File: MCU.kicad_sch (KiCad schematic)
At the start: 33 parts, among them J200 SWD, J201 USB_B_Micro, SW200 SW_SPDT, U200 STM32F405RGT6, U201 USBLC6-2SC6, Y200 16MHz

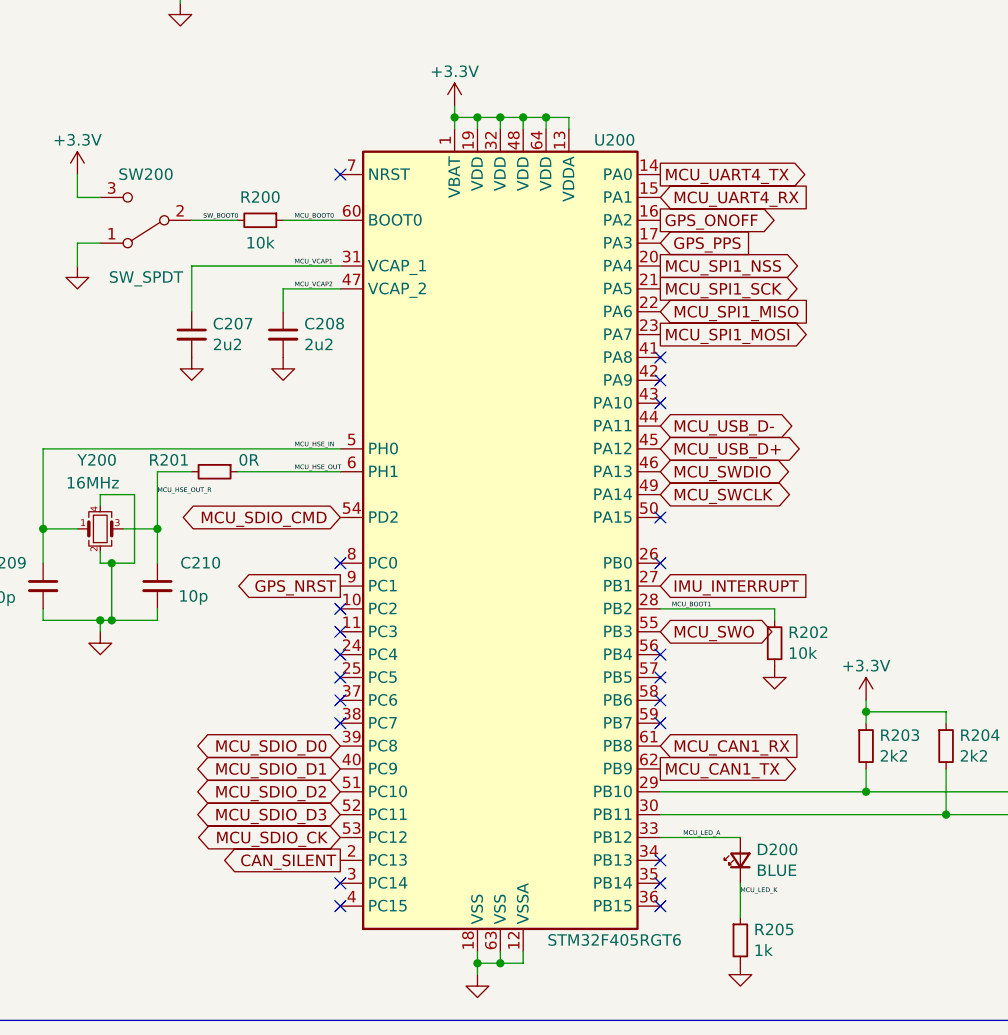
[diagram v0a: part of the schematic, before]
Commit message: replaced CAN transceiver, introduced new IMU
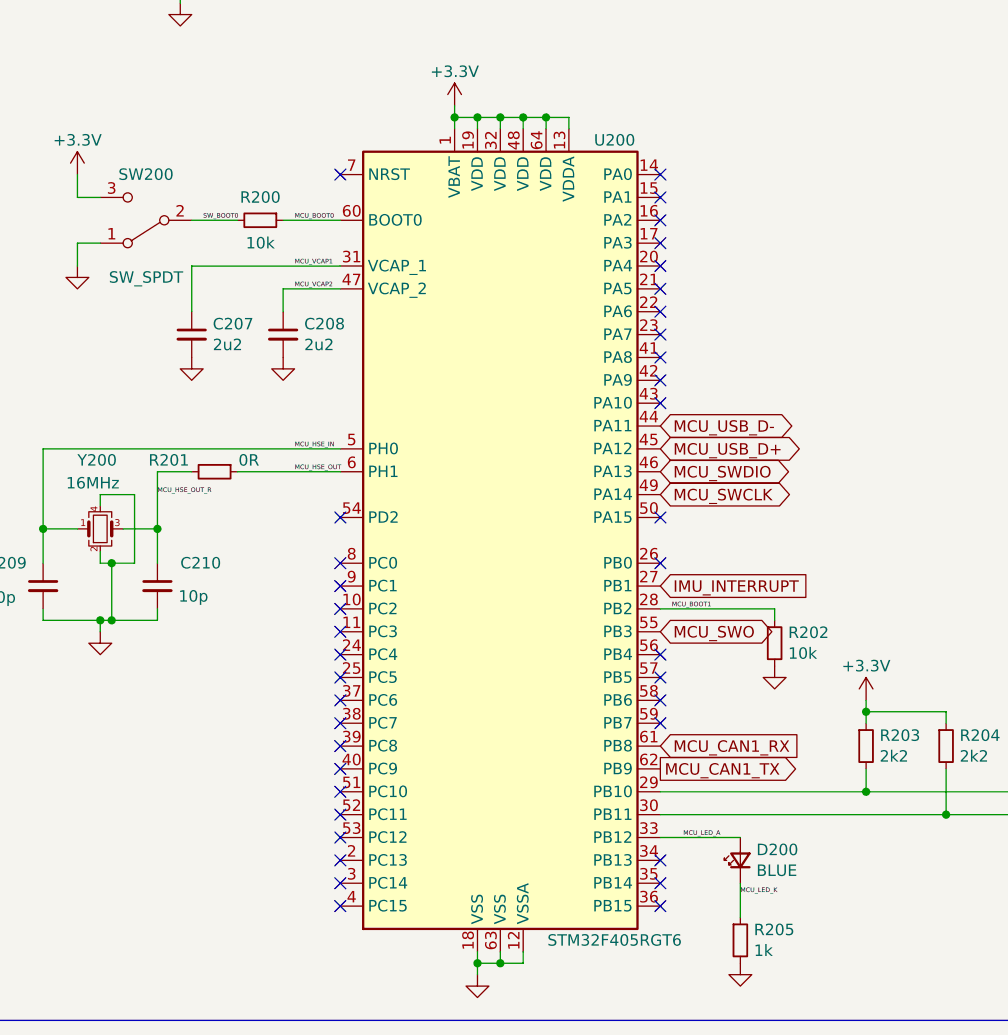
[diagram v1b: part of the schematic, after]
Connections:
- net CAN_SILENT: no longer names the net of U200.2 (PC13)
- net GPS_NRST: no longer names the net of U200.9 (PC1)
- net GPS_ONOFF: no longer names the net of U200.16 (PA2)
- net GPS_PPS: no longer names the net of U200.17 (PA3)
- net MCU_SDIO_CK: no longer names the net of U200.53 (PC12)
- net MCU_SDIO_CMD: no longer names the net of U200.54 (PD2)
- net MCU_SDIO_D0: no longer names the net of U200.39 (PC8)
- net MCU_SDIO_D1: no longer names the net of U200.40 (PC9)
- net MCU_SDIO_D2: no longer names the net of U200.51 (PC10)
- net MCU_SDIO_D3: no longer names the net of U200.52 (PC11)
- net MCU_SPI1_MISO: no longer names the net of U200.22 (PA6)
- net MCU_SPI1_MOSI: no longer names the net of U200.23 (PA7)
- net MCU_SPI1_NSS: no longer names the net of U200.20 (PA4)
- net MCU_SPI1_SCK: no longer names the net of U200.21 (PA5)
- net MCU_UART4_RX: no longer names the net of U200.15 (PA1)
- net MCU_UART4_TX: no longer names the net of U200.14 (PA0)
- no-connect marks 27 -> 43
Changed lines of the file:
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@@
   (no_connect (at 213.36 60.96))
   (no_connect (at 101.6 134.62))
+  (no_connect (at 66.04 116.84))
+  (no_connect (at 66.04 124.46))
+  (no_connect (at 66.04 142.24))
+  (no_connect (at 66.04 144.78))
+  (no_connect (at 66.04 147.32))
+  (no_connect (at 66.04 149.86))
+  (no_connect (at 66.04 152.4))
+  (no_connect (at 66.04 154.94))
+  (no_connect (at 101.6 86.36))
+  (no_connect (at 101.6 88.9))
+  (no_connect (at 101.6 91.44))
+  (no_connect (at 101.6 93.98))
+  (no_connect (at 101.6 96.52))
+  (no_connect (at 101.6 78.74))
+  (no_connect (at 101.6 81.28))
+  (no_connect (at 101.6 83.82))
   (no_connect (at 101.6 137.16))
   (no_connect (at 101.6 99.06))
@@
     )
   )
-  (global_label "MCU_SDIO_D1" (shape bidirectional) (at 66.04 144.78 180) (fields_autoplaced)
-    (effects (font (size 1.27 1.27)) (justify right))
-    (property "Intersheet References" "${INTERSHEET_REFS}" (id 0) (at 0 0 0)
-      (effects (font (size 1.27 1.27)) hide)
-    )
-  )
-  (global_label "MCU_UART4_TX" (shape output) (at 101.6 78.74 0) (fields_autoplaced)
-    (effects (font (size 1.27 1.27)) (justify left))
-    (property "Intersheet References" "${INTERSHEET_REFS}" (id 0) (at 0 0 0)
-      (effects (font (size 1.27 1.27)) hide)
-    )
-  )
   (global_label "MCU_SWO" (shape bidirectional) (at 254 55.88 0) (fields_autoplaced)
     (effects (font (size 1.27 1.27)) (justify left))
@@
     )
   )
-  (global_label "GPS_PPS" (shape input) (at 101.6 86.36 0) (fields_autoplaced)
-    (effects (font (size 1.27 1.27)) (justify left))
-    (property "Intersheet References" "${INTERSHEET_REFS}" (id 0) (at 0 0 0)
-      (effects (font (size 1.27 1.27)) hide)
-    )
-  )
   (global_label "MCU_CAN1_RX" (shape input) (at 101.6 142.24 0) (fields_autoplaced)
     (effects (font (size 1.27 1.27)) (justify left))
@@
     )
   )
-  (global_label "GPS_ONOFF" (shape output) (at 101.6 83.82 0) (fields_autoplaced)
-    (effects (font (size 1.27 1.27)) (justify left))
-    (property "Intersheet References" "${INTERSHEET_REFS}" (id 0) (at 0 0 0)
-      (effects (font (size 1.27 1.27)) hide)
-    )
-  )
   (global_label "MCU_SWO" (shape bidirectional) (at 101.6 129.54 0) (fields_autoplaced)
     (effects (font (size 1.27 1.27)) (justify left))
@@
   )
   (global_label "MCU_SWDIO" (shape bidirectional) (at 254 50.8 0) (fields_autoplaced)
-    (effects (font (size 1.27 1.27)) (justify left))
-    (property "Intersheet References" "${INTERSHEET_REFS}" (id 0) (at 0 0 0)
-      (effects (font (size 1.27 1.27)) hide)
-    )
-  )
-  (global_label "MCU_SDIO_D0" (shape bidirectional) (at 66.04 142.24 180) (fields_autoplaced)
-    (effects (font (size 1.27 1.27)) (justify right))
-    (property "Intersheet References" "${INTERSHEET_REFS}" (id 0) (at 0 0 0)
-      (effects (font (size 1.27 1.27)) hide)
-    )
-  )
-  (global_label "MCU_SDIO_D3" (shape bidirectional) (at 66.04 149.86 180) (fields_autoplaced)
-    (effects (font (size 1.27 1.27)) (justify right))
-    (property "Intersheet References" "${INTERSHEET_REFS}" (id 0) (at 0 0 0)
-      (effects (font (size 1.27 1.27)) hide)
-    )
-  )
-  (global_label "CAN_SILENT" (shape output) (at 66.04 154.94 180) (fields_autoplaced)
-    (effects (font (size 1.27 1.27)) (justify right))
-    (property "Intersheet References" "${INTERSHEET_REFS}" (id 0) (at 0 0 0)
-      (effects (font (size 1.27 1.27)) hide)
-    )
-  )
-  (global_label "MCU_UART4_RX" (shape input) (at 101.6 81.28 0) (fields_autoplaced)
     (effects (font (size 1.27 1.27)) (justify left))
     (property "Intersheet References" "${INTERSHEET_REFS}" (id 0) (at 0 0 0)
@@
     )
   )
-  (global_label "GPS_NRST" (shape output) (at 66.04 124.46 180) (fields_autoplaced)
-    (effects (font (size 1.27 1.27)) (justify right))
-    (property "Intersheet References" "${INTERSHEET_REFS}" (id 0) (at 0 0 0)
-      (effects (font (size 1.27 1.27)) hide)
-    )
-  )
   (global_label "CONN_USB_D+" (shape input) (at 252.73 118.11 180) (fields_autoplaced)
     (effects (font (size 1.27 1.27)) (justify right))
@@
     )
   )
-  (global_label "MCU_SPI1_MOSI" (shape output) (at 101.6 96.52 0) (fields_autoplaced)
-    (effects (font (size 1.27 1.27)) (justify left))
-    (property "Intersheet References" "${INTERSHEET_REFS}" (id 0) (at 0 0 0)
-      (effects (font (size 1.27 1.27)) hide)
-    )
-  )
-  (global_label "MCU_SPI1_SCK" (shape output) (at 101.6 91.44 0) (fields_autoplaced)
-    (effects (font (size 1.27 1.27)) (justify left))
-    (property "Intersheet References" "${INTERSHEET_REFS}" (id 0) (at 0 0 0)
-      (effects (font (size 1.27 1.27)) hide)
-    )
-  )
   (global_label "IMU_INTERRUPT" (shape input) (at 101.6 124.46 0) (fields_autoplaced)
     (effects (font (size 1.27 1.27)) (justify left))
@@
     )
   )
-  (global_label "MCU_SDIO_CMD" (shape bidirectional) (at 66.04 116.84 180) (fields_autoplaced)
-    (effects (font (size 1.27 1.27)) (justify right))
-    (property "Intersheet References" "${INTERSHEET_REFS}" (id 0) (at 0 0 0)
-      (effects (font (size 1.27 1.27)) hide)
-    )
-  )
   (global_label "MCU_I2C2_SDA" (shape bidirectional) (at 142.24 149.86 0) (fields_autoplaced)
     (effects (font (size 1.27 1.27)) (justify left))
@@
     )
   )
-  (global_label "MCU_SPI1_MISO" (shape input) (at 101.6 93.98 0) (fields_autoplaced)
-    (effects (font (size 1.27 1.27)) (justify left))
-    (property "Intersheet References" "${INTERSHEET_REFS}" (id 0) (at 0 0 0)
-      (effects (font (size 1.27 1.27)) hide)
-    )
-  )
   (global_label "MCU_USB_D+" (shape input) (at 210.82 116.84 0) (fields_autoplaced)
     (effects (font (size 1.27 1.27)) (justify left))
@@
     )
   )
-  (global_label "MCU_SDIO_D2" (shape bidirectional) (at 66.04 147.32 180) (fields_autoplaced)
-    (effects (font (size 1.27 1.27)) (justify right))
-    (property "Intersheet References" "${INTERSHEET_REFS}" (id 0) (at 0 0 0)
-      (effects (font (size 1.27 1.27)) hide)
-    )
-  )
-  (global_label "MCU_SDIO_CK" (shape bidirectional) (at 66.04 152.4 180) (fields_autoplaced)
-    (effects (font (size 1.27 1.27)) (justify right))
-    (property "Intersheet References" "${INTERSHEET_REFS}" (id 0) (at 0 0 0)
-      (effects (font (size 1.27 1.27)) hide)
-    )
-  )
   (global_label "MCU_SWCLK" (shape bidirectional) (at 254 53.34 0) (fields_autoplaced)
     (effects (font (size 1.27 1.27)) (justify left))
@@
     (effects (font (size 1.27 1.27)) (justify left))
     (property "Intersheet References" "${INTERSHEET_REFS}" (id 0) (at 0 0 0)
-      (effects (font (size 1.27 1.27)) hide)
-    )
-  )
-  (global_label "MCU_SPI1_NSS" (shape output) (at 101.6 88.9 0) (fields_autoplaced)
-    (effects (font (size 1.27 1.27)) (justify left))
-    (property "Intersheet References" "${INTERSHEET_REFS}" (id 0) (at 0 0 0)

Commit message: more changes!
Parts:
- added R1, R2: 2k2, Resistor_SMD:R_0402_1005Metric, symbol Device:R_Small
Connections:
- net +3V3: now also R1.1, R2.1
- net MCU_I2C1_SCL: now reaches U200.58 (PB6)
- net MCU_I2C1_SCL: now also R1.2
- net MCU_I2C1_SDA: now reaches U200.59 (PB7)
- net MCU_I2C1_SDA: now also R2.2
- no-connect marks 43 -> 41
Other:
- moved on the sheet: R202, R203, R204

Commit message: this is a message
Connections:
- net 14: now reaches U200.14 (PA0)
- net 15: now reaches U200.15 (PA1)
- net 16: now reaches U200.16 (PA2)
- net 17: now reaches U200.17 (PA3)
- net 20: now reaches U200.20 (PA4)
- net 21: now reaches U200.21 (PA5)
- net 22: now reaches U200.22 (PA6)
- net 23: now reaches U200.23 (PA7)
- net 24: now reaches U200.24 (PC4)
- net 25: now reaches U200.25 (PC5)
- net 26: now reaches U200.26 (PB0)
- net 41: now reaches U200.41 (PA8)
- net 42: now reaches U200.42 (PA9)
- net 43: now reaches U200.43 (PA10)
- net 50: now reaches U200.50 (PA15)
- no-connect marks 41 -> 26
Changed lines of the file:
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@@
   (no_connect (at 66.04 152.4))
   (no_connect (at 66.04 154.94))
-  (no_connect (at 101.6 86.36))
-  (no_connect (at 101.6 88.9))
-  (no_connect (at 101.6 91.44))
-  (no_connect (at 101.6 93.98))
-  (no_connect (at 101.6 96.52))
-  (no_connect (at 101.6 78.74))
-  (no_connect (at 101.6 81.28))
-  (no_connect (at 101.6 83.82))
-  (no_connect (at 101.6 99.06))
-  (no_connect (at 66.04 132.08))
   (no_connect (at 252.73 123.19))
   (no_connect (at 101.6 160.02))
-  (no_connect (at 101.6 101.6))
   (no_connect (at 200.66 58.42))
-  (no_connect (at 101.6 121.92))
   (no_connect (at 66.04 160.02))
   (no_connect (at 66.04 157.48))
@@
   (no_connect (at 66.04 137.16))
   (no_connect (at 213.36 58.42))
-  (no_connect (at 66.04 134.62))
-  (no_connect (at 101.6 116.84))
   (no_connect (at 66.04 129.54))
   (no_connect (at 101.6 157.48))
-  (no_connect (at 101.6 104.14))
   (no_connect (at 66.04 139.7))
   (no_connect (at 101.6 132.08))
@@
     (effects (font (size 0.508 0.508)) (justify left bottom))
   )
+  (global_label "50" (shape input) (at 101.6 116.84 0) (fields_autoplaced)
+    (effects (font (size 1.27 1.27)) (justify left))
+    (property "Intersheet References" "${INTERSHEET_REFS}" (id 0) (at 106.3432 116.7606 0)
+      (effects (font (size 1.27 1.27)) (justify left) hide)
+    )
+  )
   (global_label "MCU_CAN1_TX" (shape output) (at 101.6 144.78 0) (fields_autoplaced)
     (effects (font (size 1.27 1.27)) (justify left))
@@
     )
   )
+  (global_label "16" (shape input) (at 101.6 83.82 0) (fields_autoplaced)
+    (effects (font (size 1.27 1.27)) (justify left))
+    (property "Intersheet References" "${INTERSHEET_REFS}" (id 0) (at 106.3432 83.7406 0)
+      (effects (font (size 1.27 1.27)) (justify left) hide)
+    )
+  )
   (global_label "MCU_SWO" (shape bidirectional) (at 254 55.88 0) (fields_autoplaced)
     (effects (font (size 1.27 1.27)) (justify left))
@@
     )
   )
+  (global_label "22" (shape input) (at 101.6 93.98 0) (fields_autoplaced)
+    (effects (font (size 1.27 1.27)) (justify left))
+    (property "Intersheet References" "${INTERSHEET_REFS}" (id 0) (at 106.3432 93.9006 0)
+      (effects (font (size 1.27 1.27)) (justify left) hide)
+    )
+  )
   (global_label "MCU_SWO" (shape bidirectional) (at 101.6 129.54 0) (fields_autoplaced)
     (effects (font (size 1.27 1.27)) (justify left))
@@
     (property "Intersheet References" "${INTERSHEET_REFS}" (id 0) (at 0 0 0)
       (effects (font (size 1.27 1.27)) hide)
+    )
+  )
+  (global_label "14" (shape input) (at 101.6 78.74 0) (fields_autoplaced)
+    (effects (font (size 1.27 1.27)) (justify left))
+    (property "Intersheet References" "${INTERSHEET_REFS}" (id 0) (at 106.3432 78.6606 0)
+      (effects (font (size 1.27 1.27)) (justify left) hide)
     )
   )
@@
     )
   )
+  (global_label "17" (shape input) (at 101.6 86.36 0) (fields_autoplaced)
+    (effects (font (size 1.27 1.27)) (justify left))
+    (property "Intersheet References" "${INTERSHEET_REFS}" (id 0) (at 106.3432 86.2806 0)
+      (effects (font (size 1.27 1.27)) (justify left) hide)
+    )
+  )
   (global_label "CONN_USB_D+" (shape input) (at 252.73 118.11 180) (fields_autoplaced)
     (effects (font (size 1.27 1.27)) (justify right))
@@
     )
   )
+  (global_label "25" (shape input) (at 66.04 134.62 180) (fields_autoplaced)
+    (effects (font (size 1.27 1.27)) (justify right))
+    (property "Intersheet References" "${INTERSHEET_REFS}" (id 0) (at 61.2968 134.5406 0)
+      (effects (font (size 1.27 1.27)) (justify right) hide)
+    )
+  )
   (global_label "MCU_USB_D+" (shape bidirectional) (at 101.6 109.22 0) (fields_autoplaced)
     (effects (font (size 1.27 1.27)) (justify left))
     (property "Intersheet References" "${INTERSHEET_REFS}" (id 0) (at 0 0 0)
       (effects (font (size 1.27 1.27)) hide)
+    )
+  )
+  (global_label "26" (shape input) (at 101.6 121.92 0) (fields_autoplaced)
+    (effects (font (size 1.27 1.27)) (justify left))
+    (property "Intersheet References" "${INTERSHEET_REFS}" (id 0) (at 106.3432 121.8406 0)
+      (effects (font (size 1.27 1.27)) (justify left) hide)
+    )
+  )
+  (global_label "43" (shape input) (at 101.6 104.14 0) (fields_autoplaced)
+    (effects (font (size 1.27 1.27)) (justify left))
+    (property "Intersheet References" "${INTERSHEET_REFS}" (id 0) (at 106.3432 104.0606 0)
+      (effects (font (size 1.27 1.27)) (justify left) hide)
     )
   )
@@
     )
   )
+  (global_label "41" (shape input) (at 101.6 99.06 0) (fields_autoplaced)
+    (effects (font (size 1.27 1.27)) (justify left))
+    (property "Intersheet References" "${INTERSHEET_REFS}" (id 0) (at 106.3432 98.9806 0)
+      (effects (font (size 1.27 1.27)) (justify left) hide)
+    )
+  )
+  (global_label "21" (shape input) (at 101.6 91.44 0) (fields_autoplaced)
+    (effects (font (size 1.27 1.27)) (justify left))
+    (property "Intersheet References" "${INTERSHEET_REFS}" (id 0) (at 106.3432 91.3606 0)
+      (effects (font (size 1.27 1.27)) (justify left) hide)
+    )
+  )
   (global_label "MCU_I2C2_SDA" (shape bidirectional) (at 142.24 158.75 0) (fields_autoplaced)
     (effects (font (size 1.27 1.27)) (justify left))
@@
     )
   )
+  (global_label "20" (shape input) (at 101.6 88.9 0) (fields_autoplaced)
+    (effects (font (size 1.27 1.27)) (justify left))
+    (property "Intersheet References" "${INTERSHEET_REFS}" (id 0) (at 106.3432 88.8206 0)
+      (effects (font (size 1.27 1.27)) (justify left) hide)
+    )
+  )
+  (global_label "42" (shape input) (at 101.6 101.6 0) (fields_autoplaced)
+    (effects (font (size 1.27 1.27)) (justify left))
+    (property "Intersheet References" "${INTERSHEET_REFS}" (id 0) (at 106.3432 101.5206 0)
+      (effects (font (size 1.27 1.27)) (justify left) hide)
+    )
+  )
   (global_label "MCU_USB_D+" (shape input) (at 210.82 116.84 0) (fields_autoplaced)
     (effects (font (size 1.27 1.27)) (justify left))
@@
     )
   )
+  (global_label "15" (shape input) (at 101.6 81.28 0) (fields_autoplaced)
+    (effects (font (size 1.27 1.27)) (justify left))
+    (property "Intersheet References" "${INTERSHEET_REFS}" (id 0) (at 106.3432 81.2006 0)
+      (effects (font (size 1.27 1.27)) (justify left) hide)
+    )
+  )
   (global_label "MCU_SWCLK" (shape bidirectional) (at 254 53.34 0) (fields_autoplaced)
     (effects (font (size 1.27 1.27)) (justify left))
     (property "Intersheet References" "${INTERSHEET_REFS}" (id 0) (at 0 0 0)
       (effects (font (size 1.27 1.27)) hide)
+    )
+  )
+  (global_label "24" (shape input) (at 66.04 132.08 180) (fields_autoplaced)
+    (effects (font (size 1.27 1.27)) (justify right))
+    (property "Intersheet References" "${INTERSHEET_REFS}" (id 0) (at 61.2968 132.0006 0)
+      (effects (font (size 1.27 1.27)) (justify right) hide)
     )
   )
@@
     )
   )
+  (global_label "23" (shape input) (at 101.6 96.52 0) (fields_autoplaced)
+    (effects (font (size 1.27 1.27)) (justify left))
+    (property "Intersheet References" "${INTERSHEET_REFS}" (id 0) (at 106.3432 96.4406 0)
+      (effects (font (size 1.27 1.27)) (justify left) hide)
+    )
+  )
